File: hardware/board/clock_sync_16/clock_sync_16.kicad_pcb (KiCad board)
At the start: 4 copper layers, 36 x 28 mm, 47 parts, among them J2 AudioJack3, J3 USB_C_Receptacle_USB2.0, U1 TPD2EUSB30, U2 LP2985-3.3, U3 RP2040, U4 W25Q16JVUXIQ, X1 ECS-TXO-2016

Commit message: route pcb v0.1
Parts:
- removed the REF** at (160.0, 84.0)
- removed the REF** at (128.0, 108.0)
- removed the REF** at (160.0, 108.0)
- removed the REF** at (128.0, 84.0)
- added ?: , , F.Cu at (117.0, 38.0)
- added ?: , , F.Cu at (171.0, 38.0)
- added C1: 1uF, Capacitor_SMD:C_0402_1005Metric, F.Cu at (133.4, 47.6)
- added C24: 1uF, Capacitor_SMD:C_0402_1005Metric, F.Cu at (133.4, 69.4)
- added C25: 1uF, Capacitor_SMD:C_0402_1005Metric, F.Cu at (133.4, 80.4)
- added C26: 1uF, Capacitor_SMD:C_0402_1005Metric, F.Cu at (131.6, 73.5)
- added C27: 1uF, Capacitor_SMD:C_0402_1005Metric, F.Cu at (131.6, 84.4)
- added C28: 1uF, Capacitor_SMD:C_0402_1005Metric, F.Cu at (133.4, 91.3)
- added C29: 1uF, Capacitor_SMD:C_0402_1005Metric, F.Cu at (133.4, 102.2)
- added C3: 1uF, Capacitor_SMD:C_0402_1005Metric, F.Cu at (131.6, 51.6)
- added C30: 1uF, Capacitor_SMD:C_0402_1005Metric, F.Cu at (133.4, 113.1)
- added C31: 1uF, Capacitor_SMD:C_0402_1005Metric, F.Cu at (133.4, 124.0)
- added C32: 1uF, Capacitor_SMD:C_0402_1005Metric, F.Cu at (131.6, 95.3)
- added C33: 1uF, Capacitor_SMD:C_0402_1005Metric, F.Cu at (131.6, 106.2)
- added C34: 1uF, Capacitor_SMD:C_0402_1005Metric, F.Cu at (131.6, 117.2)
- added C35: 1uF, Capacitor_SMD:C_0402_1005Metric, F.Cu at (131.6, 128.1)
- added C36: 1uF, Capacitor_SMD:C_0402_1005Metric, F.Cu at (154.6, 53.0)
- added C37: 1uF, Capacitor_SMD:C_0402_1005Metric, F.Cu at (154.6, 64.1)
- added C38: 1uF, Capacitor_SMD:C_0402_1005Metric, F.Cu at (154.6, 75.0)
- added C39: 1uF, Capacitor_SMD:C_0402_1005Metric, F.Cu at (154.6, 86.1)
- added C40: 1uF, Capacitor_SMD:C_0402_1005Metric, F.Cu at (156.4, 48.9)
- added C41: 1uF, Capacitor_SMD:C_0402_1005Metric, F.Cu at (156.4, 59.9)
- added C42: 1uF, Capacitor_SMD:C_0402_1005Metric, F.Cu at (156.4, 70.9)
- added C43: 1uF, Capacitor_SMD:C_0402_1005Metric, F.Cu at (156.4, 81.9)
- added C44: 1uF, Capacitor_SMD:C_0402_1005Metric, F.Cu at (154.6, 97.0)
- added C45: 1uF, Capacitor_SMD:C_0402_1005Metric, F.Cu at (154.6, 108.0)
- added C46: 1uF, Capacitor_SMD:C_0402_1005Metric, F.Cu at (154.6, 119.0)
- added C47: 1uF, Capacitor_SMD:C_0402_1005Metric, F.Cu at (154.6, 130.1)
- added C48: 1uF, Capacitor_SMD:C_0402_1005Metric, F.Cu at (156.4, 92.9)
- added C49: 1uF, Capacitor_SMD:C_0402_1005Metric, F.Cu at (156.4, 103.8)
- added C5: 1uF, Capacitor_SMD:C_0402_1005Metric, F.Cu at (133.4, 58.4)
- added C50: 1uF, Capacitor_SMD:C_0402_1005Metric, F.Cu at (156.4, 114.9)
- added C51: 1uF, Capacitor_SMD:C_0402_1005Metric, F.Cu at (156.4, 125.9)
- added C52: 1uF, Capacitor_SMD:C_0402_1005Metric, F.Cu at (135.3, 132.8)
- added C53: 1uF, Capacitor_SMD:C_0402_1005Metric, F.Cu at (135.6, 138.9)
- added C54: 1uF, Capacitor_SMD:C_0402_1005Metric, F.Cu at (150.5, 114.2)
- added C7: 1uF, Capacitor_SMD:C_0402_1005Metric, F.Cu at (131.6, 62.6)
- added D10: D_TVS, Diode_SMD:D_0402_1005Metric, F.Cu at (133.1, 85.9)
- added D11: LED, LED_SMD:LED_0603_1608Metric_Pad1.05x0.95mm_HandSolder, F.Cu at (130.3, 72.4)
- added D12: LED, LED_SMD:LED_0603_1608Metric_Pad1.05x0.95mm_HandSolder, F.Cu at (130.3, 83.3)
- added D13: D_TVS, Diode_SMD:D_0402_1005Metric, F.Cu at (133.1, 96.9)
- added D14: D_TVS, Diode_SMD:D_0402_1005Metric, F.Cu at (154.8, 47.3)
- added D15: D_TVS, Diode_SMD:D_0402_1005Metric, F.Cu at (154.8, 58.3)
- added D16: D_TVS, Diode_SMD:D_0402_1005Metric, F.Cu at (154.8, 69.3)
- added D17: D_TVS, Diode_SMD:D_0402_1005Metric, F.Cu at (154.8, 80.3)
- added D18: LED, LED_SMD:LED_0603_1608Metric_Pad1.05x0.95mm_HandSolder, F.Cu at (157.7, 50.0)
- added D19: LED, LED_SMD:LED_0603_1608Metric_Pad1.05x0.95mm_HandSolder, F.Cu at (157.7, 61.0)
- added D20: LED, LED_SMD:LED_0603_1608Metric_Pad1.05x0.95mm_HandSolder, F.Cu at (157.7, 72.0)
- added D21: LED, LED_SMD:LED_0603_1608Metric_Pad1.05x0.95mm_HandSolder, F.Cu at (157.7, 83.0)
- added D22: LED, LED_SMD:LED_0603_1608Metric_Pad1.05x0.95mm_HandSolder, F.Cu at (130.3, 50.5)
- added D23: D_TVS, Diode_SMD:D_0402_1005Metric, F.Cu at (133.1, 107.8)
- added D24: D_TVS, Diode_SMD:D_0402_1005Metric, F.Cu at (133.1, 118.7)
- added D25: D_TVS, Diode_SMD:D_0402_1005Metric, F.Cu at (133.2, 129.6)
- added D26: LED, LED_SMD:LED_0603_1608Metric_Pad1.05x0.95mm_HandSolder, F.Cu at (130.3, 94.2)
- added D27: LED, LED_SMD:LED_0603_1608Metric_Pad1.05x0.95mm_HandSolder, F.Cu at (130.3, 105.1)
- added D28: LED, LED_SMD:LED_0603_1608Metric_Pad1.05x0.95mm_HandSolder, F.Cu at (130.3, 116.1)
- added D29: LED, LED_SMD:LED_0603_1608Metric_Pad1.05x0.95mm_HandSolder, F.Cu at (130.3, 127.0)
- added D30: D_TVS, Diode_SMD:D_0402_1005Metric, F.Cu at (154.8, 91.3)
- added D31: D_TVS, Diode_SMD:D_0402_1005Metric, F.Cu at (154.8, 102.3)
- added D32: D_TVS, Diode_SMD:D_0402_1005Metric, F.Cu at (154.8, 113.3)
- added D33: D_TVS, Diode_SMD:D_0402_1005Metric, F.Cu at (154.8, 124.3)
- added D34: LED, LED_SMD:LED_0603_1608Metric_Pad1.05x0.95mm_HandSolder, F.Cu at (157.7, 94.0)
- added D35: LED, LED_SMD:LED_0603_1608Metric_Pad1.05x0.95mm_HandSolder, F.Cu at (157.7, 105.0)
- added D36: LED, LED_SMD:LED_0603_1608Metric_Pad1.05x0.95mm_HandSolder, F.Cu at (157.7, 116.0)
- added D37: LED, LED_SMD:LED_0603_1608Metric_Pad1.05x0.95mm_HandSolder, F.Cu at (157.7, 127.0)
- added D38: LED, LED_SMD:LED_0603_1608Metric_Pad1.05x0.95mm_HandSolder, F.Cu at (120.2, 135.4)
- added D39: D_TVS, Diode_SMD:D_0402_1005Metric, F.Cu at (134.5, 138.9)
- added D6: D_TVS, Diode_SMD:D_0402_1005Metric, F.Cu at (133.1, 53.2)
- added D7: D_TVS, Diode_SMD:D_0402_1005Metric, F.Cu at (133.1, 64.1)
- added D8: LED, LED_SMD:LED_0603_1608Metric_Pad1.05x0.95mm_HandSolder, F.Cu at (130.3, 61.4)
- added D9: D_TVS, Diode_SMD:D_0402_1005Metric, F.Cu at (133.1, 75.0)
- added J1: AudioJack3, kicad_component_library:Jack_3.5mm_Kycon_STX-3680-5NB_Vertical, F.Cu at (121.5, 50.0)
- added J10: AudioJack3, kicad_component_library:Jack_3.5mm_Kycon_STX-3680-5NB_Vertical, F.Cu at (121.5, 127.0)
- added J11: AudioJack3, kicad_component_library:Jack_3.5mm_Kycon_STX-3680-5NB_Vertical, F.Cu at (166.5, 50.0)
- added J12: AudioJack3, kicad_component_library:Jack_3.5mm_Kycon_STX-3680-5NB_Vertical, F.Cu at (166.5, 61.0)
- added J13: AudioJack3, kicad_component_library:Jack_3.5mm_Kycon_STX-3680-5NB_Vertical, F.Cu at (166.5, 72.0)
- added J14: AudioJack3, kicad_component_library:Jack_3.5mm_Kycon_STX-3680-5NB_Vertical, F.Cu at (166.5, 83.0)
- added J15: AudioJack3, kicad_component_library:Jack_3.5mm_Kycon_STX-3680-5NB_Vertical, F.Cu at (166.5, 94.0)
- added J16: AudioJack3, kicad_component_library:Jack_3.5mm_Kycon_STX-3680-5NB_Vertical, F.Cu at (166.5, 105.0)
- added J17: AudioJack3, kicad_component_library:Jack_3.5mm_Kycon_STX-3680-5NB_Vertical, F.Cu at (166.5, 116.0)
- added J18: AudioJack3, kicad_component_library:Jack_3.5mm_Kycon_STX-3680-5NB_Vertical, F.Cu at (166.5, 127.0)
- added J19: Conn_01x03_Male, Connector_PinHeader_2.54mm:PinHeader_1x03_P2.54mm_Vertical, F.Cu at (141.4, 102.5)
- added J20: Conn_01x03_Female, Connector_Phoenix_MC:PhoenixContact_MCV_1,5_3-G-3.5_1x03_P3.50mm_Vertical, F.Cu at (124.0, 138.5)
- added J4: AudioJack3, kicad_component_library:Jack_3.5mm_Kycon_STX-3680-5NB_Vertical, F.Cu at (121.5, 61.0)
- added J5: AudioJack3, kicad_component_library:Jack_3.5mm_Kycon_STX-3680-5NB_Vertical, F.Cu at (121.5, 72.0)
- added J6: AudioJack3, kicad_component_library:Jack_3.5mm_Kycon_STX-3680-5NB_Vertical, F.Cu at (121.5, 83.0)
- added J7: AudioJack3, kicad_component_library:Jack_3.5mm_Kycon_STX-3680-5NB_Vertical, F.Cu at (121.5, 94.0)
- added J8: AudioJack3, kicad_component_library:Jack_3.5mm_Kycon_STX-3680-5NB_Vertical, F.Cu at (121.5, 105.0)
- added J9: AudioJack3, kicad_component_library:Jack_3.5mm_Kycon_STX-3680-5NB_Vertical, F.Cu at (121.5, 116.0)
- added R13: R, Resistor_SMD:R_0402_1005Metric, F.Cu at (131.6, 93.2)
- added R14: R, Resistor_SMD:R_0402_1005Metric, F.Cu at (131.6, 104.0)
- added R15: R, Resistor_SMD:R_0402_1005Metric, F.Cu at (131.6, 115.0)
- added R16: R, Resistor_SMD:R_0402_1005Metric, F.Cu at (131.6, 125.9)
- added R17: R, Resistor_SMD:R_0402_1005Metric, F.Cu at (156.4, 51.1)
- added R18: R, Resistor_SMD:R_0402_1005Metric, F.Cu at (156.4, 62.1)
- added R19: R, Resistor_SMD:R_0402_1005Metric, F.Cu at (156.4, 73.1)
- added R20: R, Resistor_SMD:R_0402_1005Metric, F.Cu at (156.4, 84.1)
- added R21: R, Resistor_SMD:R_0402_1005Metric, F.Cu at (156.4, 95.0)
- added R22: R, Resistor_SMD:R_0402_1005Metric, F.Cu at (156.4, 106.1)
- added R23: R, Resistor_SMD:R_0402_1005Metric, F.Cu at (156.4, 117.1)
- added R24: R, Resistor_SMD:R_0402_1005Metric, F.Cu at (156.4, 128.1)
- added R25: R, Resistor_SMD:R_0402_1005Metric, F.Cu at (121.0, 133.1)
- added R4: R, Resistor_SMD:R_0402_1005Metric, F.Cu at (131.6, 49.4)
- added R5: R, Resistor_SMD:R_0402_1005Metric, F.Cu at (131.6, 60.4)
- added R6: R, Resistor_SMD:R_0402_1005Metric, F.Cu at (131.6, 71.3)
- added R7: R, Resistor_SMD:R_0402_1005Metric, F.Cu at (131.6, 82.2)
- added REF**: MountingHole_3.2mm_M3_DIN965, MountingHole:MountingHole_3.2mm_M3_DIN965, F.Cu at (117.0, 38.0)
- added REF**: MountingHole_3.2mm_M3_DIN965, MountingHole:MountingHole_3.2mm_M3_DIN965, F.Cu at (117.0, 139.0)
- added REF**: MountingHole_3.2mm_M3_DIN965, MountingHole:MountingHole_3.2mm_M3_DIN965, F.Cu at (171.0, 38.0)
- added REF**: MountingHole_3.2mm_M3_DIN965, MountingHole:MountingHole_3.2mm_M3_DIN965, F.Cu at (171.0, 139.0)
- added U10: ISO6521FREUR, kicad_component_library:DFN-8_3x2mm_P0.5mm, F.Cu at (133.4, 105.1)
- added U11: ISO6521FREUR, kicad_component_library:DFN-8_3x2mm_P0.5mm, F.Cu at (133.4, 116.1)
- added U12: ISO6521FREUR, kicad_component_library:DFN-8_3x2mm_P0.5mm, F.Cu at (133.4, 127.0)
- added U13: ISO6521FREUR, kicad_component_library:DFN-8_3x2mm_P0.5mm, F.Cu at (154.6, 50.0)
- added U14: ISO6521FREUR, kicad_component_library:DFN-8_3x2mm_P0.5mm, F.Cu at (154.6, 61.0)
- added U15: ISO6521FREUR, kicad_component_library:DFN-8_3x2mm_P0.5mm, F.Cu at (154.6, 72.0)
- added U16: ISO6521FREUR, kicad_component_library:DFN-8_3x2mm_P0.5mm, F.Cu at (154.6, 83.0)
- added U17: ISO6521FREUR, kicad_component_library:DFN-8_3x2mm_P0.5mm, F.Cu at (154.6, 94.0)
- added U18: ISO6521FREUR, kicad_component_library:DFN-8_3x2mm_P0.5mm, F.Cu at (154.6, 105.0)
- added U19: ISO6521FREUR, kicad_component_library:DFN-8_3x2mm_P0.5mm, F.Cu at (154.6, 116.0)
- added U20: ISO6521FREUR, kicad_component_library:DFN-8_3x2mm_P0.5mm, F.Cu at (154.6, 127.0)
- added U21: SN74LVC1G125DCK, Package_TO_SOT_SMD:Texas_R-PDSO-G5_DCK-5, F.Cu at (150.5, 116.2)
- added U22: ISO6521FREUR, kicad_component_library:DFN-8_3x2mm_P0.5mm, F.Cu at (135.3, 135.8)
- added U5: ISO6521FREUR, kicad_component_library:DFN-8_3x2mm_P0.5mm, F.Cu at (133.4, 50.5)
- added U6: ISO6521FREUR, kicad_component_library:DFN-8_3x2mm_P0.5mm, F.Cu at (133.4, 61.4)
- added U7: ISO6521FREUR, kicad_component_library:DFN-8_3x2mm_P0.5mm, F.Cu at (133.4, 72.4)
- added U8: ISO6521FREUR, kicad_component_library:DFN-8_3x2mm_P0.5mm, F.Cu at (133.4, 83.3)
- added U9: ISO6521FREUR, kicad_component_library:DFN-8_3x2mm_P0.5mm, F.Cu at (133.4, 94.2)
- J2: moved to B.Cu
- moved FID3 79.9 mm to (167.0, 38.0)
- moved FID2 57.0 mm to (167.0, 139.0)
- moved FID1 54.0 mm to (117.0, 135.0)
- moved SW2 44.0 mm to (144.0, 128.0), turned to -90 degrees
- moved R1 42.8 mm to (146.4, 126.2)
- moved C10 42.5 mm to (165.1, 137.2)
- moved D1 42.5 mm to (164.1, 137.2)
- moved R8 41.8 mm to (147.6, 122.8), turned to 180 degrees
- moved C12 41.2 mm to (149.8, 125.8), turned to 0 degrees
- moved C8 39.4 mm to (145.2, 122.2), turned to 90 degrees
- moved C19 39.0 mm to (144.2, 122.2), turned to 90 degrees
- moved U4 38.5 mm to (147.6, 121.0), turned to 180 degrees
- moved C21 36.9 mm to (150.2, 127.3), turned to 0 degrees
- moved D5 36.6 mm to (150.1, 133.2), turned to 180 degrees
- moved U2 36.3 mm to (149.8, 129.9)
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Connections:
- net +3V3 renamed +3.3V
- net /Harp Core RP2040 + USB/HARP_CLK_SYNC renamed /Harp Core RP2040 + USB/HARP_CLKIN_SYNC
- U3 pad 11: unconnected-(U3-GPIO8-Pad11) -> /Clock Outputs 8 - 16/CH8_CONNECTED
- U3 pad 12: unconnected-(U3-GPIO9-Pad12) -> /Clock Outputs 8 - 16/CH9_CONNECTED
- U3 pad 13: unconnected-(U3-GPIO10-Pad13) -> /Clock Outputs 8 - 16/CH10_CONNECTED
- U3 pad 14: unconnected-(U3-GPIO11-Pad14) -> /Clock Outputs 8 - 16/CH11_CONNECTED
- U3 pad 15: unconnected-(U3-GPIO12-Pad15) -> /Clock Outputs 8 - 16/CH12_CONNECTED
- U3 pad 16: unconnected-(U3-GPIO13-Pad16) -> /Clock Outputs 8 - 16/CH13_CONNECTED
- U3 pad 17: unconnected-(U3-GPIO14-Pad17) -> /Clock Outputs 8 - 16/CH14_CONNECTED
- U3 pad 18: unconnected-(U3-GPIO15-Pad18) -> /Clock Outputs 8 - 16/CH15_CONNECTED
- U3 pad 2: unconnected-(U3-GPIO0-Pad2) -> /Harp Core RP2040 + USB/SLOW_CLKOUT
- U3 pad 27: unconnected-(U3-GPIO16-Pad27) -> /Clock Outputs 0 - 7/CH0_CONNECTED
- U3 pad 28: unconnected-(U3-GPIO17-Pad28) -> /Clock Outputs 0 - 7/CH1_CONNECTED
- U3 pad 29: unconnected-(U3-GPIO18-Pad29) -> /Clock Outputs 0 - 7/CH2_CONNECTED
- U3 pad 3: unconnected-(U3-GPIO1-Pad3) -> /Harp Core RP2040 + USB/UART0_RXD
- U3 pad 30: unconnected-(U3-GPIO19-Pad30) -> /Clock Outputs 0 - 7/CH3_CONNECTED
- U3 pad 31: unconnected-(U3-GPIO20-Pad31) -> /Clock Outputs 0 - 7/CH4_CONNECTED
- U3 pad 32: unconnected-(U3-GPIO21-Pad32) -> /Clock Outputs 0 - 7/CH5_CONNECTED
- U3 pad 34: unconnected-(U3-GPIO22-Pad34) -> /Clock Outputs 0 - 7/CH6_CONNECTED
- U3 pad 35: unconnected-(U3-GPIO23-Pad35) -> /Clock Outputs 0 - 7/CH7_CONNECTED
- U3 pad 4: unconnected-(U3-GPIO2-Pad4) -> /Harp Core RP2040 + USB/SLOW_CLKOUT_CONNECTED
- U3 pad 6: unconnected-(U3-GPIO4-Pad6) -> /Harp Core RP2040 + USB/HARP_CLKOUT
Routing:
- net HARP_CLKOUT: track 0.00 -> 196.3 mm, vias 0 -> 16
- net /Clock Outputs 8 - 16/CH8_CONNECTED: track 0.00 -> 67.6 mm, vias 0 -> 1
- net /Clock Outputs 0 - 7/CH0_CONNECTED: track 0.00 -> 66.3 mm, vias 0 -> 1
- net /Clock Outputs 8 - 16/CH9_CONNECTED: track 0.00 -> 56.9 mm, vias 0 -> 2
- net /Clock Outputs 0 - 7/CH1_CONNECTED: track 0.00 -> 55.6 mm, vias 0 -> 1
- net /Clock Outputs 8 - 16/CH10_CONNECTED: track 0.00 -> 45.7 mm, vias 0 -> 2
- net /Clock Outputs 0 - 7/CH2_CONNECTED: track 0.00 -> 44.4 mm, vias 0 -> 1
- net /Harp Core RP2040 + USB/SLOW_CLKOUT: track 0.00 -> 43.6 mm, vias 0 -> 2
- net +3.3V: track 38.6 -> 80.2 mm, vias 16 -> 38
- net GND: track 32.4 -> 72.4 mm, vias 28 -> 53
- net /Clock Outputs 0 - 7/CH3_CONNECTED: track 0.00 -> 35.1 mm, vias 0 -> 1
- net /Clock Outputs 8 - 16/CH11_CONNECTED: track 0.00 -> 34.4 mm, vias 0 -> 2
- net Net-(J20-Pin_2): track 0.00 -> 29.7 mm
- net /Harp Core RP2040 + USB/SLOW_CLKOUT_CONNECTED: track 0.00 -> 28.3 mm, vias 0 -> 2
- net /Clock Outputs 0 - 7/CH4_CONNECTED: track 0.00 -> 23.9 mm, vias 0 -> 1
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- added copper zone on In2.Cu, net +1V1
- added copper zone on In1.Cu, net Net-(D10-A1)
- added copper zone on In1.Cu, net Net-(D11-K)
- added copper zone on In1.Cu, net Net-(D13-A1)
- added copper zone on In1.Cu, net Net-(D14-A1)
- added copper zone on In1.Cu, net Net-(D15-A1)
- added copper zone on In1.Cu, net Net-(D16-A1)
- added copper zone on In1.Cu, net Net-(D17-A1)
- added copper zone on In1.Cu, net Net-(D22-K)
- added copper zone on In1.Cu, net Net-(D23-A1)
- added copper zone on In1.Cu, net Net-(D24-A1)
- added copper zone on In1.Cu, net Net-(D25-A1)
- added copper zone on In1.Cu, net Net-(D30-A1)
- added copper zone on In1.Cu, net Net-(D31-A1)
- added copper zone on In1.Cu, net Net-(D32-A1)
- added copper zone on In1.Cu, net Net-(D33-A1)
- added copper zone on In1.Cu, net Net-(D38-K)
- added copper zone on In1.Cu, net Net-(D7-A1)
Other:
- board size 36 x 28 mm -> 60 x 107 mm
- board text added: "CLK"
- board text added: "GND1"
- board text added: "May 30, 2024"
- board text added: "Sonya Vasquez"
- board text added: "V0.1.0"
- board text added: "VCC1"
- board text removed: "1"
- board text removed: "V0.1.1"

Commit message: draft v0.1 pcb
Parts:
- removed ? (x2): , 
- removed the REF** at (117.0, 38.0)
- removed the REF** at (117.0, 139.0)
- removed the REF** at (171.0, 139.0)
- added REF**: MountingHole_3.2mm_M3_DIN965, MountingHole:MountingHole_3.2mm_M3_DIN965, F.Cu at (140.0, 75.0)
- added REF**: MountingHole_3.2mm_M3_DIN965, MountingHole:MountingHole_3.2mm_M3_DIN965, F.Cu at (167.0, 138.0)
- added REF**: MountingHole_3.2mm_M3_DIN965, MountingHole:MountingHole_3.2mm_M3_DIN965, F.Cu at (140.0, 100.0)
- added REF**: MountingHole_3.2mm_M3_DIN965, MountingHole:MountingHole_3.2mm_M3_DIN965, F.Cu at (113.0, 37.0)
- added REF**: MountingHole_3.2mm_M3_DIN965, MountingHole:MountingHole_3.2mm_M3_DIN965, F.Cu at (113.0, 138.0)
- U2: value LP2985-3.3 -> TPS73433DDCR
- moved J19 54.6 mm to (137.5, 48.0)
- moved C23 4.28 mm to (143.4, 127.8)
- moved D5 4.27 mm to (146.0, 132.2)
- moved D2 4.22 mm to (143.9, 132.2)
- moved R2 4.20 mm to (137.5, 132.6)
- moved C16 4.19 mm to (133.7, 112.8)
- moved C47 4.19 mm to (150.6, 128.8)
- moved C37 4.16 mm to (150.6, 63.0)
- moved C39 4.14 mm to (150.6, 85.0)
- moved C36 4.14 mm to (150.6, 52.0)
- moved C38 4.14 mm to (150.6, 74.0)
- moved C44 4.14 mm to (150.6, 96.0)
- moved C45 4.14 mm to (150.6, 107.0)
- moved C46 4.14 mm to (150.6, 118.0)
- moved D11 4.12 mm to (126.3, 71.4)
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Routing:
- net /Harp Core RP2040 + USB/SLOW_CLKOUT: track 43.6 -> 102.3 mm
- net /Harp Core RP2040 + USB/UART0_RXD: track 17.0 -> 71.6 mm
- net /Harp Core RP2040 + USB/SLOW_CLKOUT_CONNECTED: track 28.3 -> 32.1 mm
- net GND: track 72.4 -> 73.7 mm, vias 53 -> 55
- net +3.3V: track 80.2 -> 79.2 mm, vias 38 -> 39
- net /Clock Outputs 0 - 7/CH1_CONNECTED: track 55.6 -> 55.2 mm, vias 1 -> 0
- net /Clock Outputs 0 - 7/CH6_CONNECTED: track 8.08 -> 7.93 mm, vias 1 -> 0
- net /Clock Outputs 0 - 7/CH7_CONNECTED: vias 1 -> 0
- net /Clock Outputs 0 - 7/CH5_CONNECTED: vias 1 -> 0
- net /Clock Outputs 8 - 16/CH8_CONNECTED: vias 1 -> 0
- net /Clock Outputs 0 - 7/CH4_CONNECTED: vias 1 -> 0
- net /Clock Outputs 0 - 7/CH3_CONNECTED: vias 1 -> 0
- net /Clock Outputs 0 - 7/CH2_CONNECTED: vias 1 -> 0
- net /Clock Outputs 0 - 7/CH0_CONNECTED: vias 1 -> 0
- added copper zone on B.Cu, net HARP_CLKOUT
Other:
- board text added: "0"
- board text added: "1"
- board text added: "10"
- board text added: "11"
- board text added: "12"
- board text added: "13"
- board text added: "14"
- board text added: "15"
- board text added: "2"
- board text added: "3"
- board text added: "4"
- board text added: "5"
- board text added: "6"
- board text added: "7"
- board text added: "8"
- board text added: "9"
- board text added: "GND"
- board text added: "May 31, 2024"
- board text added: "RX"
- board text added: "Slow CLKOUT (J20) ↓"
- board text added: "TODO: QR Code"
- board text added: "TX"
- board text added: "harp.device.white-rabbit"
- board text removed: "May 30, 2024"

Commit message: draft firmware
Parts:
- added G***: LOGO, LOGO, B.Cu at (140.0, 60.6)
- C1, C24, C25, C26, C27, C28, C29, C3, C30, C31, C32, C33, C34, C35, C36, C37, C38, C39, C40, C41, C42, C43, C44, C45, C46, C47, C48, C49, C5, C50, C51, C52, C53, C7: value 1uF -> 100nF
- R13, R14, R15, R16, R17, R18, R19, R20, R21, R22, R23, R24, R25, R4, R5, R6, R7: value R -> 330
- moved J19 1.50 mm to (137.5, 46.5)
- moved C31 0.15 mm to (129.4, 122.9), turned to 0 degrees
- turned C38 to 180 degrees
- turned C1 to 0 degrees
- turned C24 to 0 degrees
- turned C25 to 0 degrees
- turned C28 to 0 degrees
- turned C29 to 0 degrees
- turned C30 to 0 degrees
- turned C36 to 180 degrees
- turned C37 to 180 degrees
- turned C39 to 180 degrees
- turned C44 to 180 degrees
- turned C45 to 180 degrees
- turned C46 to 180 degrees
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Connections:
- C1 pad 1: +3.3V -> GND
- C1 pad 2: GND -> +3.3V
- C24 pad 1: +3.3V -> GND
- C24 pad 2: GND -> +3.3V
- C25 pad 1: +3.3V -> GND
- C25 pad 2: GND -> +3.3V
- C28 pad 1: +3.3V -> GND
- C28 pad 2: GND -> +3.3V
- C29 pad 1: +3.3V -> GND
- C29 pad 2: GND -> +3.3V
- C30 pad 1: +3.3V -> GND
- C30 pad 2: GND -> +3.3V
- C31 pad 1: +3.3V -> GND
- C31 pad 2: GND -> +3.3V
- C36 pad 1: +3.3V -> GND
- C36 pad 2: GND -> +3.3V
- C37 pad 1: +3.3V -> GND
- C37 pad 2: GND -> +3.3V
- C38 pad 1: +3.3V -> GND
- C38 pad 2: GND -> +3.3V
- C39 pad 1: +3.3V -> GND
- C39 pad 2: GND -> +3.3V
- C44 pad 1: +3.3V -> GND
- C44 pad 2: GND -> +3.3V
- C45 pad 1: +3.3V -> GND
- C45 pad 2: GND -> +3.3V
- C46 pad 1: +3.3V -> GND
- C46 pad 2: GND -> +3.3V
- C47 pad 1: +3.3V -> GND
- C47 pad 2: GND -> +3.3V
- C5 pad 1: +3.3V -> GND
- C5 pad 2: GND -> +3.3V
- C52 pad 1: +3.3V -> GND
- C52 pad 2: GND -> +3.3V
- C53 pad 1: Net-(J20-Pin_2) -> Net-(D38-K)
- C53 pad 2: Net-(D38-K) -> Net-(J20-Pin_2)
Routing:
- net /Harp Core RP2040 + USB/UART0_RXD: track 71.6 -> 73.1 mm
- net /Harp Core RP2040 + USB/SLOW_CLKOUT: track 102.3 -> 103.8 mm
- net HARP_CLKOUT: track 196.3 -> 197.5 mm
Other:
- board text added: "16-channel-output Harp time keeper and synchronizer."
- board text added: "Debug Output (TX shared with Slow CLKOUT) ↓"
- board text added: "June 4, 2024"
- board text added: "Source Files and Setup ↓"
- board text removed: "May 31, 2024"
- board text removed: "TODO: QR Code"

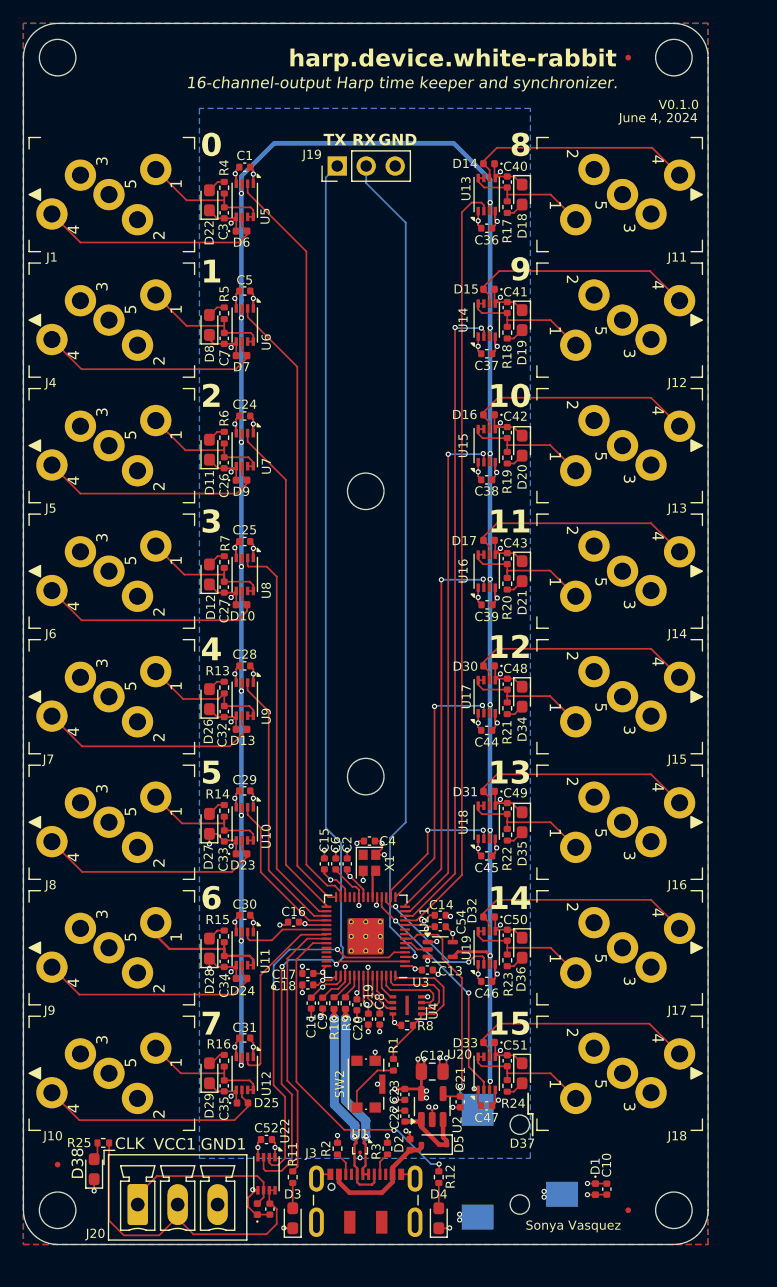
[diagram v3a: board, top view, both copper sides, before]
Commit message: add pps/slow_uart output options
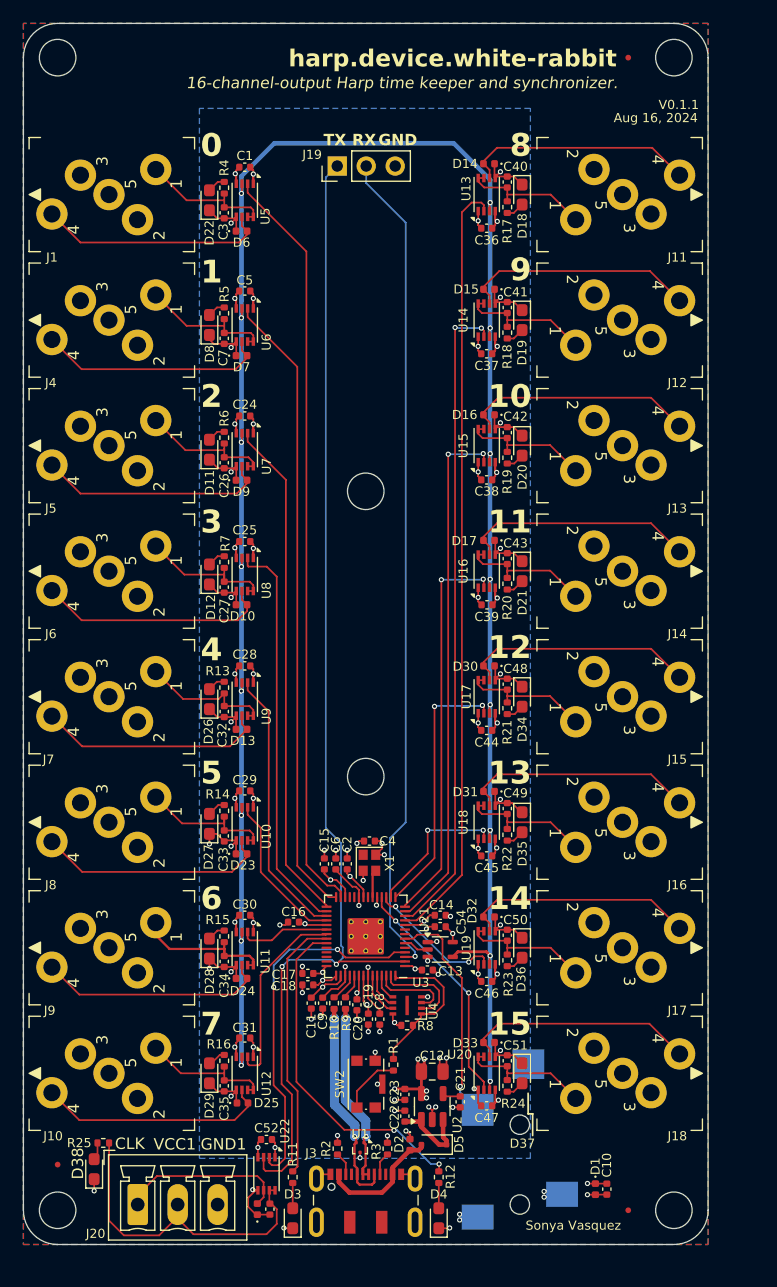
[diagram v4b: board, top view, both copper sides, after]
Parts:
- J2: footprint Connector_Audio:Jack_3.5mm_CUI_SJ-3523-SMT_Horizontal -> Connector_Audio:Jack_3.5mm_CUI_SJ-3524-SMT_Horizontal
- R13, R14, R15, R16, R17, R18, R19, R20, R21, R22, R23, R24, R25, R4, R5, R6, R7: value 330 -> 1K6
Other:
- board text added: "Aug 16, 2024"
- board text added: "V0.1.1"
- board text removed: "June 4, 2024"
- board text removed: "V0.1.0"

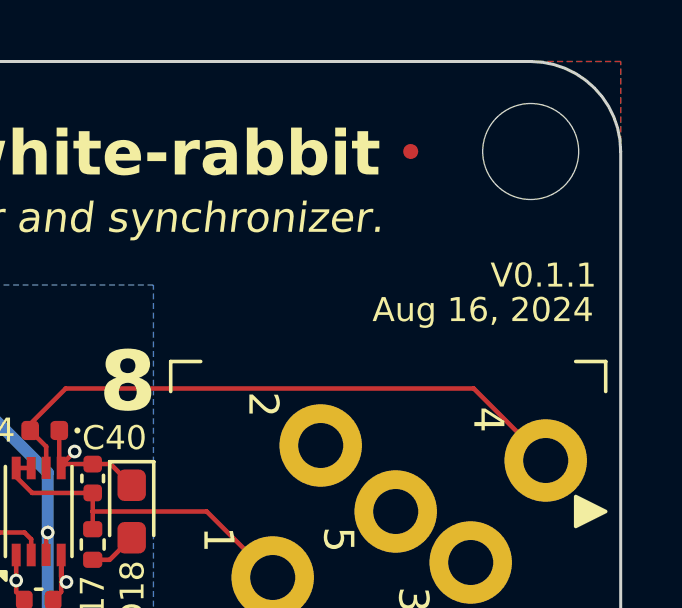
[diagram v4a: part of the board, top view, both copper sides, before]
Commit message: update harp core; update led resistors and deprecated parts; bump versions
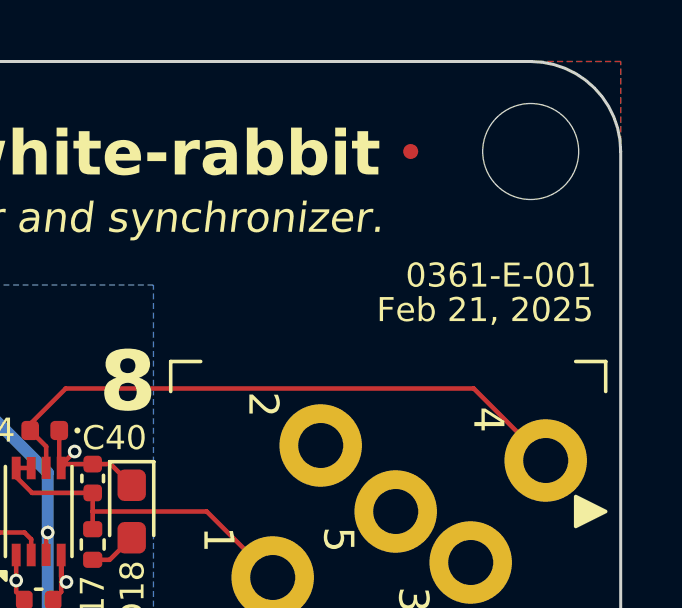
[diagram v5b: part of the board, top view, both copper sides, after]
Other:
- board text added: "0361-E-001"
- board text added: "Feb 21, 2025"
- board text removed: "Aug 16, 2024"
- board text removed: "V0.1.1"
